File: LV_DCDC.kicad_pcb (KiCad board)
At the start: 2 copper layers, 109 parts, among them J101 1017503, J102 1017503, J201 5023860270, J202 Conn_01x05, J203 Conn_01x04, J204 Conn_01x04, U201 STM32G431KBT6, U301 TCAN1462VDRQ1, U302 ESDCAN24-2BLY, U401 LMR50410YFQDBVRQ1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

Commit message: progress on layout in general, minor tweaks to schemas
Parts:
- added C208: 4.7uF, Capacitor_SMD:C_0603_1608Metric, B.Cu at (126.8, 158.2)
- C201, C202, C203: footprint Capacitor_SMD:C_0805_2012Metric -> Capacitor_SMD:C_0603_1608Metric; moved to B.Cu
- C204, C205, C206, C207, C301, C302, C303, J201, J202, J204, L201, R201, R202, R203, R204, R205, R206, R301, R302, TH201, U201, U301, U302, Y201: moved to B.Cu
- moved R109 172.6 mm to (276.9, 97.0)
- moved R110 172.6 mm to (276.9, 99.5)
- moved R111 172.6 mm to (276.9, 102.0)
- moved C501 171.6 mm to (230.7, 49.5)
- moved C502 171.6 mm to (230.7, 52.0)
- moved C503 171.6 mm to (230.7, 54.5)
- moved C504 171.6 mm to (230.7, 57.1)
- moved R501 171.6 mm to (230.7, 59.6)
- moved R502 171.6 mm to (230.7, 62.1)
- moved R503 171.6 mm to (230.7, 64.6)
- moved R504 171.6 mm to (230.7, 67.1)
- moved U501 171.6 mm to (236.2, 50.6)
- moved U502 171.6 mm to (236.2, 55.2)
- moved C114 166.2 mm to (276.5, 106.8)
- moved R202 109.4 mm to (158.5, 161.2), turned to 90 degrees
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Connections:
- D101 pad 1: Net-(D101-K) -> GNDPWR
- J203 pad 1: +3.3V -> GNDA
- J203 pad 2: SWDIO -> SWCLK
- J203 pad 3: SWCLK -> SWDIO
- J203 pad 4: GNDA -> +3.3V
- R105 pad 2: Net-(D101-K) -> GNDPWR
- U302 pad 1: /uC/CAN/CANH -> /uC/CAN/CANL
- U302 pad 2: /uC/CAN/CANL -> /uC/CAN/CANH
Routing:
- net /uC/CAN/CANL: track 0.00 -> 31.5 mm
- net /uC/CAN/CANH: track 0.00 -> 31.5 mm
- net +3.3V: track 0.00 -> 18.1 mm
- net Net-(U201-VDDA/VREF+): track 0.00 -> 6.84 mm
- net GNDA: track 0.00 -> 5.12 mm
- net /uC/DCM temp: track 0.00 -> 3.26 mm
- net Net-(U201-PF0-OSC_IN): track 0.00 -> 3.15 mm
- net Net-(C303-Pad2): track 0.00 -> 3.07 mm
- net I2C2_SDA: track 0.00 -> 2.88 mm
- net Net-(U201-PB8-BOOT0): track 0.00 -> 2.84 mm
- net +5V: track 0.00 -> 2.83 mm
- net I2C2_SCL: track 0.00 -> 2.59 mm
- net /uC/ambient temp: track 0.00 -> 2.17 mm
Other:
- copper layers 2 -> 4

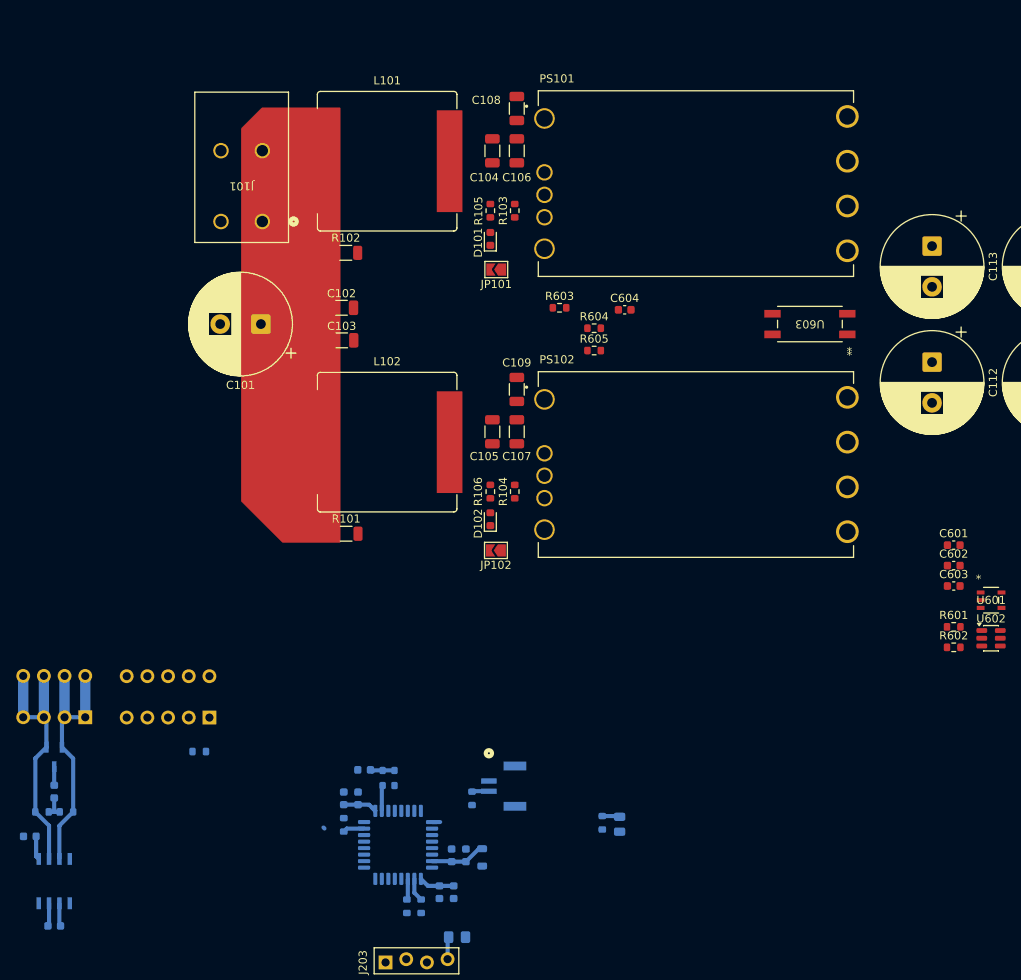
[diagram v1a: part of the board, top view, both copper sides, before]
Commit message: made heatsink holes
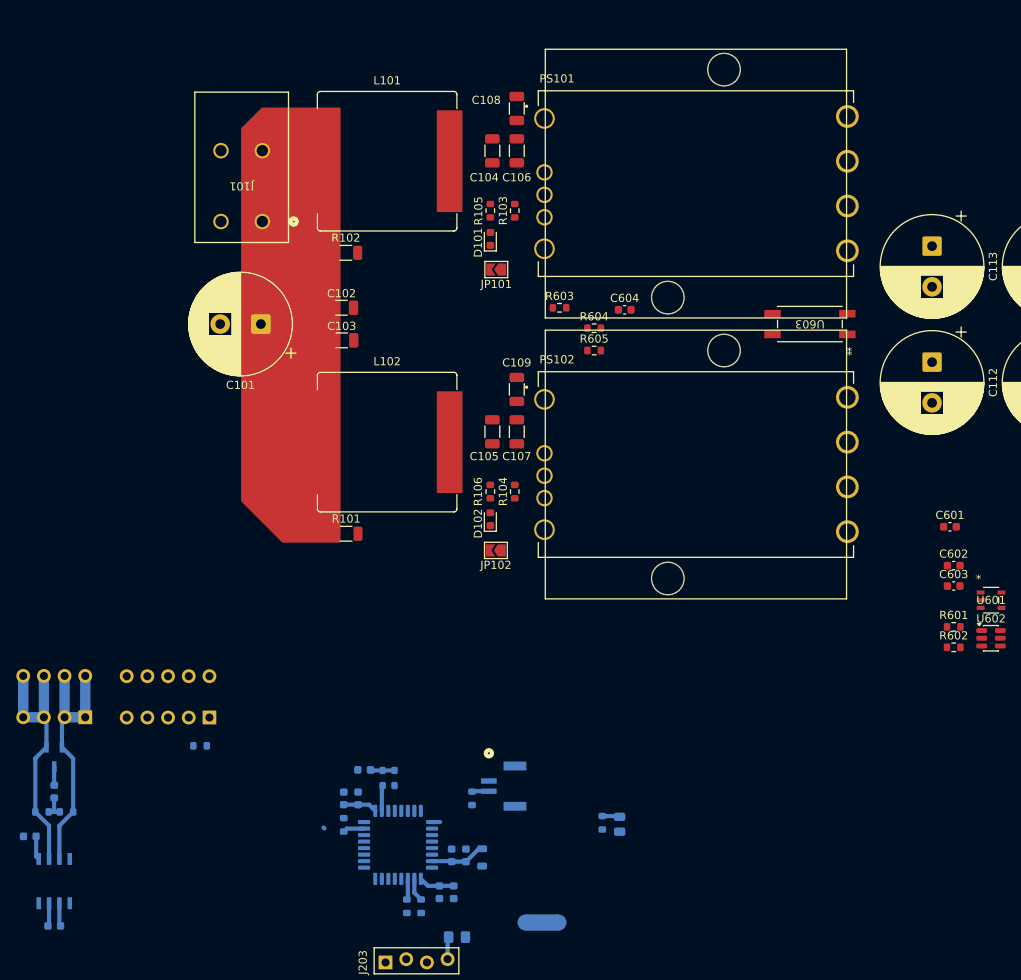
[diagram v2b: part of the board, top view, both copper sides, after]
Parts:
- added NT1: NetTie_2, NetTie:NetTie-2_SMD_Pad2.0mm, B.Cu at (151.1, 173.5)
- added REF**: libra, Library:libra, F.Cu at (170.0, 117.2)
- added REF**: libra, Library:libra, F.Cu at (170.0, 82.8)
- moved C601 2.30 mm to (201.2, 124.9)
- moved R206 0.71 mm to (109.1, 151.8)
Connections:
- C201 pad 2: GNDA -> GNDD
- C202 pad 2: GNDA -> GNDD
- C203 pad 2: GNDA -> GNDD
- C204 pad 2: GNDA -> GNDD
- C205 pad 2: GNDA -> GNDD
- C206 pad 2: GNDA -> GNDD
- C207 pad 2: GNDA -> GNDD
- C208 pad 2: GNDA -> GNDD
- C301 pad 2: GNDA -> GNDD
- C302 pad 2: GNDA -> GNDD
- C303 pad 1: GNDA -> GNDD
- C401 pad 2: GNDA -> GNDD
- C402 pad 2: GNDA -> GNDD
- C403 pad 2: GNDA -> GNDD
- C404 pad 2: GNDA -> GNDD
- C405 pad 2: GNDA -> GNDD
- C406 pad 2: GNDA -> GNDD
- C407 pad 2: GNDA -> GNDD
- C408 pad 2: GNDA -> GNDD
- C411 pad 2: GNDA -> GNDD
- C412 pad 2: GNDA -> GNDD
- C413 pad 2: GNDA -> GNDD
- C414 pad 2: GNDA -> GNDD
- J201 pad 1: GNDA -> GNDD
- J202 pad 2: GNDA -> GNDD
- J203 pad 1: GNDA -> GNDD
- R203 pad 2: GNDA -> GNDD
- R206 pad 1: GNDA -> GNDD
- R402 pad 2: GNDA -> GNDD
- R404 pad 2: GNDA -> GNDD
- TH201 pad 2: GNDA -> GNDD
- U201 pad 16: GNDA -> GNDD
- U201 pad 3: GNDA -> GNDD
- U201 pad 32: GNDA -> GNDD
- U301 pad 2: GNDA -> GNDD
- U301 pad 8: GNDA -> GNDD
- U302 pad 3: GNDA -> GNDD
- U401 pad 2: GNDA -> GNDD
- U402 pad 2: GNDA -> GNDD
- Y201 pad 2: GNDA -> GNDD
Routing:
- net GNDD: track 0.00 -> 5.12 mm
- net GNDA: track 5.12 -> 0.00 mm

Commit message: Layout done except for silkscreen
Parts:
- removed NT1: NetTie_2, NetTie:NetTie-2_SMD_Pad2.0mm
- removed REF** (x2): libra, Library:libra
- added C114: ?, Capacitor_SMD:C_1206_3216Metric, F.Cu at (184.9, 79.2)
- added C115: ?, Capacitor_SMD:C_1206_3216Metric, F.Cu at (184.9, 70.1)
- added C116: ?, Capacitor_SMD:C_1206_3216Metric, F.Cu at (184.9, 74.6)
- added NT101: NetTie_2, NetTie:NetTie-2_SMD_Pad2.0mm, B.Cu at (142.4, 84.0)
- added NT102: NetTie_2, NetTie:NetTie-2_SMD_Pad2.0mm, B.Cu at (141.8, 82.6)
- C202, C203, C204, C205, C206, J201, L201, R204, R205: moved to F.Cu
- C207: renamed from C208; moved to F.Cu
- C401, C402, C403, C404, C405, C406, C411, C412, C413, C414: footprint Capacitor_SMD:C_0603_1608Metric -> Capacitor_SMD:C_1206_3216Metric; moved to B.Cu
- C407, C408, C409, C410, L401, L402, R401, R402, R403, R404, U401, U402: moved to B.Cu
- moved C301 131.8 mm to (180.0, 76.5)
- moved C302 131.8 mm to (177.0, 65.5)
- moved C303 131.8 mm to (180.0, 60.0)
- moved J204 131.8 mm to (183.8, 50.9)
- moved R301 131.8 mm to (181.5, 62.5)
- moved R302 131.8 mm to (178.5, 62.5)
- moved U301 131.8 mm to (180.0, 71.0)
- moved R111 131.7 mm to (148.0, 75.0), turned to -90 degrees
- moved U302 131.5 mm to (180.0, 56.2)
- moved R110 128.5 mm to (150.8, 75.0), turned to -90 degrees
- moved R109 125.1 mm to (153.8, 75.0), turned to -90 degrees
- moved C117 124.0 mm to (156.6, 75.0), turned to -90 degrees
- moved C407 117.9 mm to (183.6, 92.4), turned to 90 degrees
- moved C414 116.0 mm to (168.8, 91.5), turned to 90 degrees
- moved J202 114.8 mm to (170.9, 50.9)
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- renumbered C114 to C117, C207 to C208
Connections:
- C117 pad 2: GND -> GNDA
- R111 pad 2: GND -> GNDA
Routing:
- net +5V: track 2.83 -> 188.4 mm, vias 0 -> 7
- net +3.3V: track 18.1 -> 124.7 mm, vias 0 -> 4
- net +24V: track 0.00 -> 67.8 mm, vias 0 -> 2
- net /uC/DCM temp: track 3.26 -> 52.8 mm, vias 0 -> 3
- net GNDPWR: track 0.00 -> 48.4 mm, vias 0 -> 46
- net GNDD: track 5.12 -> 47.7 mm, vias 0 -> 8
- net GNDA: track 0.00 -> 37.1 mm, vias 0 -> 167
- net Net-(R602-Pad2): track 0.00 -> 35.6 mm
- net I2C2_SCL: track 2.59 -> 37.5 mm, vias 0 -> 2
- net I2C2_SDA: track 2.88 -> 36.9 mm, vias 0 -> 2
- net /uC/ambient temp: track 2.17 -> 29.5 mm
- net TR2: track 0.00 -> 23.8 mm
- net TR1: track 0.00 -> 21.7 mm
- net Net-(JP101-A): track 0.00 -> 21.5 mm
- net Net-(JP102-A): track 0.00 -> 21.3 mm
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- added copper zone on F.Cu, net +24V
- added copper zone on F.Cu, net +VDC
- added copper zone on F.Cu, net /shunt/Shunt1+
- added copper zone on F.Cu, net /shunt/Shunt2+
- added copper zone on F.Cu, net GND
- added copper zone on In1.Cu, net GND
- added copper zone on B.Cu, net GNDA
- added copper zone on F.Cu, net GNDA
- added copper zone on In1.Cu, net GNDA
- added copper zone on In2.Cu, net GNDA
- added copper zone on B.Cu, net GNDD
- added copper zone on In2.Cu, net GNDD
- added copper zone on B.Cu, net GNDPWR
- added copper zone on F.Cu, net GNDPWR
- added copper zone on In1.Cu, net GNDPWR
- added copper zone on In2.Cu, net GNDPWR
- added copper zone on F.Cu, net Net-(PS101-+IN)
- added copper zone on F.Cu, net Net-(PS101-+OUT)
- added copper zone on F.Cu, net Net-(PS102-+IN)
- added copper zone on F.Cu, net Net-(PS102-+OUT)
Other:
- board outline added: 160 x 70 mm

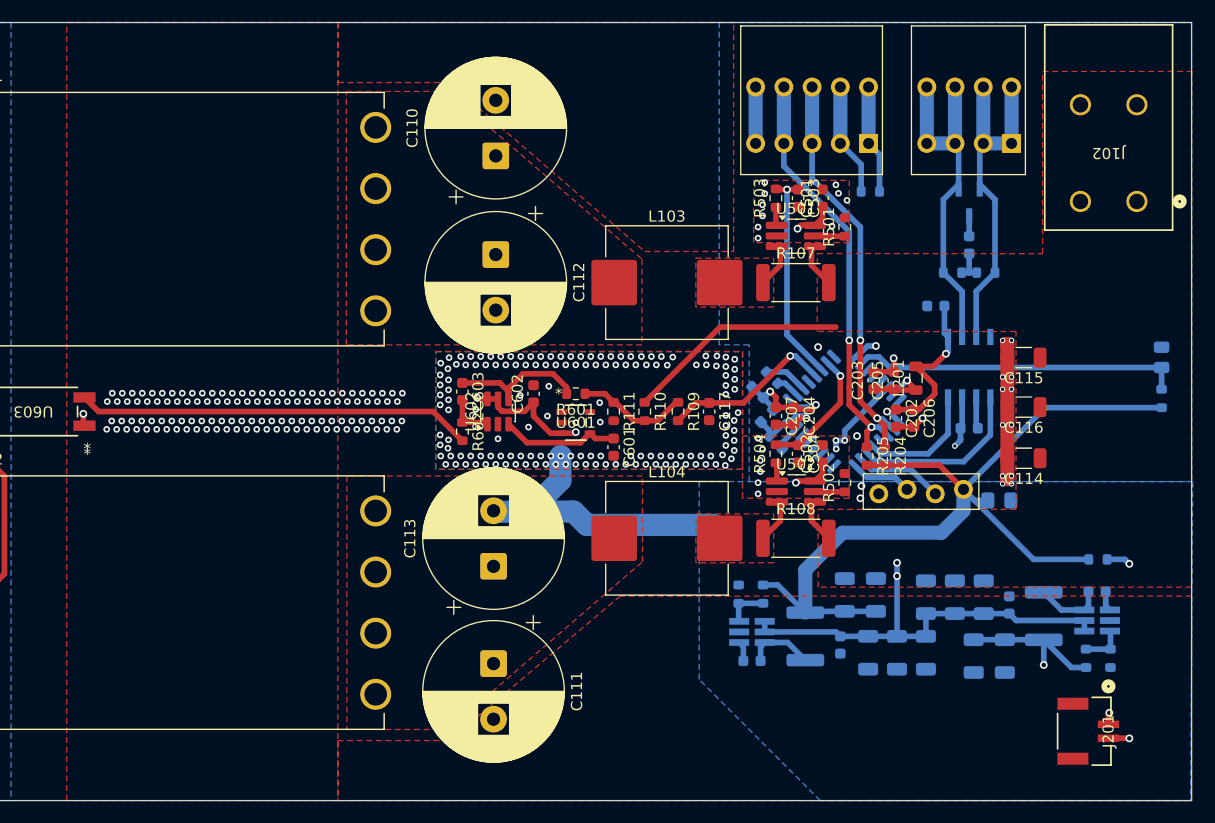
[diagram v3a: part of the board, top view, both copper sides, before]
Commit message: moved the accuracy trim to bottom side. added stitching to bottom of DCMs
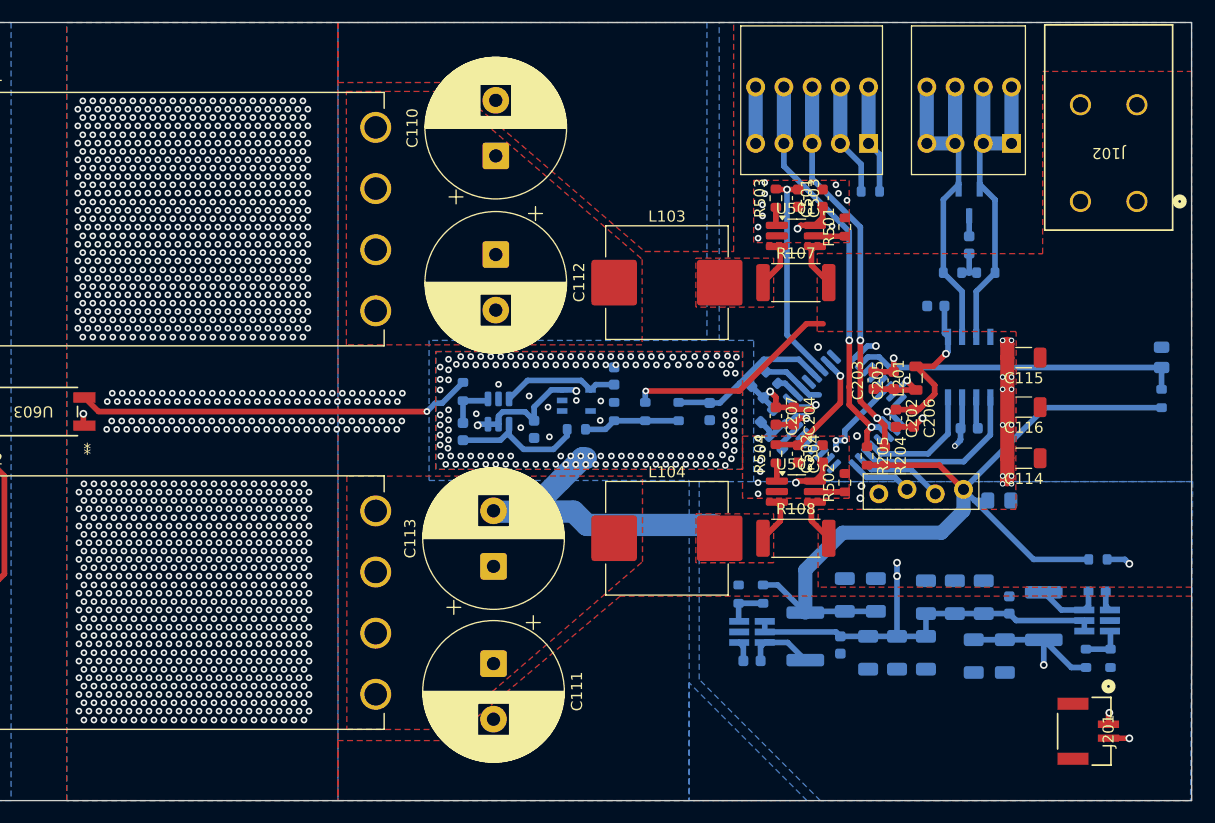
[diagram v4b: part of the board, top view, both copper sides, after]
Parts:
- C117, C601, C602, C603, R109, R110, R111, R601, R602, U601, U602: moved to B.Cu
- moved C601 6.40 mm to (148.1, 71.8), turned to 90 degrees
- moved C603 3.60 mm to (134.4, 76.8), turned to 90 degrees
- moved R602 3.60 mm to (134.4, 73.2), turned to 90 degrees
- moved R601 3.20 mm to (144.7, 76.6)
- moved C602 3.20 mm to (140.8, 76.6), turned to -90 degrees
- moved U601 2.00 mm to (144.7, 74.0)
- moved C117 0.05 mm to (156.7, 75.0)
- moved R111 0.05 mm to (148.1, 75.0), turned to 90 degrees
- moved U602 0.05 mm to (137.7, 75.0), turned to -90 degrees
- turned R109 to 90 degrees
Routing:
- net +5V: track 188.4 -> 199.0 mm
- net GNDD: track 47.7 -> 49.4 mm
- net /trim/VoltageSense: track 10.1 -> 8.70 mm
- net /uC/Vsense: track 15.5 -> 14.5 mm, vias 1 -> 0
- net GNDA: track 37.1 -> 38.0 mm, vias 167 -> 165
- net +24V: track 67.8 -> 67.3 mm, vias 2 -> 3
- net Net-(R602-Pad2): track 35.6 -> 35.7 mm, vias 0 -> 1
- net GND: vias 132 -> 1494
- added copper zone on B.Cu, net GND
- added copper zone on In2.Cu, net GND
